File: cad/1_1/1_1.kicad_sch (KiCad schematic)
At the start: 12 parts, among them J1 Conn_01x04_Pin, U1 ATtiny1616-M

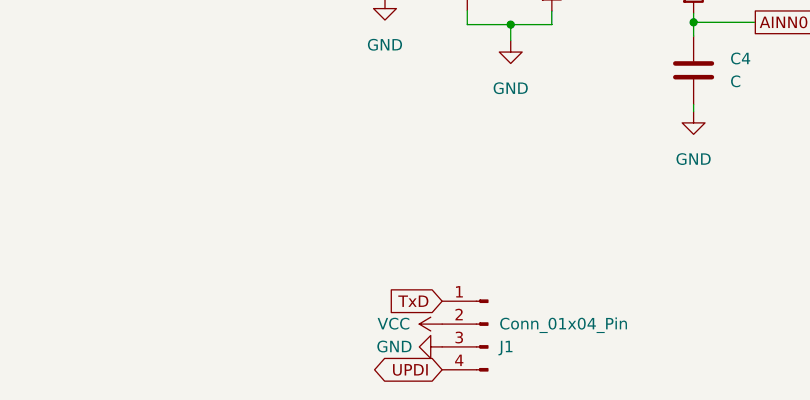
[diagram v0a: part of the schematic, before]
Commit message: 全体的に部品を左上に移動した TxDとRxDを接続した
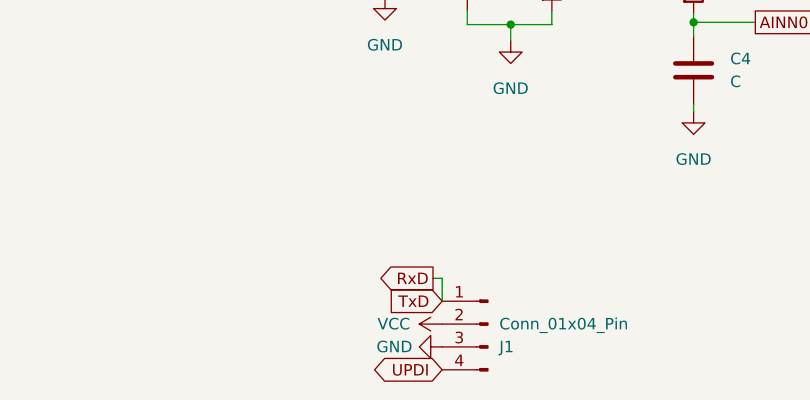
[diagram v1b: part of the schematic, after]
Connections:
- net TxD is gone; now on net RxD: J1.1 (Pin_1), U1.20 (PA1)
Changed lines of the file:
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@@
+	(wire
+		(pts
+			(xy 131.572 123.19) (xy 131.572 125.73)
+		)
+		(stroke
+			(width 0)
+			(type default)
+		)
+	)
 	(wire
 		(pts
@@
 	(wire
 		(pts
+			(xy 130.556 123.19) (xy 131.572 123.19)
+		)
+		(stroke
+			(width 0)
+			(type default)
+		)
+	)
+	(wire
+		(pts
 			(xy 125.984 56.896) (xy 133.096 56.896)
 		)
@@
 	(wire
 		(pts
+			(xy 232.156 47.244) (xy 231.14 47.244)
+		)
+		(stroke
+			(width 0)
+			(type default)
+		)
+	)
+	(wire
+		(pts
 			(xy 125.984 64.008) (xy 125.984 61.976)
 		)
@@
 		(pts
 			(xy 232.156 57.404) (xy 231.14 57.404)
-		)
-		(stroke
-			(width 0)
-			(type default)
-		)
-	)
-	(wire
-		(pts
-			(xy 232.156 47.244) (xy 231.14 47.244)
 		)
 		(stroke
@@
 		)
 	)
-	(global_label "RxD"
-		(shape input)
-		(at 231.14 49.784 0)
-		(fields_autoplaced yes)
-		(effects
-			(font
-				(size 1.27 1.27)
-			)
-			(justify left)
-		)
-		(property "Intersheetrefs" "${INTERSHEET_REFS}"
-			(at 237.6933 49.784 0)
-			(effects
-				(font
-					(size 1.27 1.27)
-				)
-				(justify left)
-				(hide yes)
-			)
-		)
-	)
 	(global_label "AINP0"
 		(shape output)
@@
 		)
 	)
+	(global_label "TxD"
+		(shape output)
+		(at 232.156 47.244 0)
+		(effects
+			(font
+				(size 1.27 1.27)
+			)
+			(justify left)
+		)
+		(property "Intersheetrefs" "${INTERSHEET_REFS}"
+			(at 232.156 47.244 0)
+			(effects
+				(font
+					(size 1.27 1.27)
+				)
+				(hide yes)
+			)
+		)
+	)
 	(global_label "SCK"
 		(shape input)
@@
 		)
 	)
+	(global_label "RxD"
+		(shape input)
+		(at 231.14 49.784 0)
+		(effects
+			(font
+				(size 1.27 1.27)
+			)
+			(justify left)
+		)
+		(property "Intersheetrefs" "${INTERSHEET_REFS}"
+			(at 231.14 49.784 0)
+			(effects
+				(font
+					(size 1.27 1.27)
+				)
+				(hide yes)
+			)
+		)
+	)
 	(global_label "MOSI"
 		(shape input)
@@
 		(property "Intersheetrefs" "${INTERSHEET_REFS}"
 			(at 193.0786 72.644 0)
-			(effects
-				(font
-					(size 1.27 1.27)
-				)
-				(justify right)
-				(hide yes)
-			)
-		)
-	)
-	(global_label "TxD"
-		(shape input)
-		(at 131.572 125.73 180)
-		(fields_autoplaced yes)
-		(effects
-			(font
-				(size 1.27 1.27)
-			)
-			(justify right)
-		)
-		(property "Intersheetrefs" "${INTERSHEET_REFS}"
-			(at 125.3211 125.73 0)
 			(effects
 				(font
@@
 	)
 	(global_label "TxD"
-		(shape output)
-		(at 232.156 47.244 0)
-		(fields_autoplaced yes)
-		(effects
-			(font
-				(size 1.27 1.27)
-			)
-			(justify left)
-		)
-		(property "Intersheetrefs" "${INTERSHEET_REFS}"
-			(at 238.4069 47.244 0)
-			(effects
-				(font
-					(size 1.27 1.27)
-				)
-				(justify left)
+		(shape input)
+		(at 131.572 125.73 180)
+		(fields_autoplaced yes)
+		(effects
+			(font
+				(size 1.27 1.27)
+			)
+			(justify right)
+		)
+		(property "Intersheetrefs" "${INTERSHEET_REFS}"
+			(at 125.3211 125.73 0)
+			(effects
+				(font
+					(size 1.27 1.27)
+				)
+				(justify right)
 				(hide yes)
 			)
@@
 				(hide yes)
 			)
+		)
+	)
+	(global_label "RxD"
+		(shape output)
+		(at 130.556 123.19 180)
+		(effects
+			(font
+				(size 1.27 1.27)
+			)
+			(justify right)
+		)
+		(property "Intersheetrefs" "${INTERSHEET_REFS}"
+			(at 130.556 123.19 0)
+			(effects
+				(font
+					(size 1.27 1.27)
+				)
+				(hide yes)
+			)
